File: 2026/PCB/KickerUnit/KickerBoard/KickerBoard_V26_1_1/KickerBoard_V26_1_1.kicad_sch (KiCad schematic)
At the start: 0 parts

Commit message: LT3751のシンボル作成
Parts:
- added U1: LT3751UFD, KickerUnit_LIB_SYM:QFN-20-1EP_LT3751UFD, symbol KickerUnit_LIB_SYM:LT3751UFD
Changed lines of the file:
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@@
 	(generator_version "9.0")
 	(paper "A4")
+	(symbol
+		(lib_id "KickerUnit_LIB_SYM:LT3751UFD")
+		(at 114.3 74.93 0)
+		(unit 1)
+		(exclude_from_sim no)
+		(in_bom yes)
+		(on_board yes)
+		(dnp no)
+		(property "Reference" "U1"
+			(at 96.774 99.568 0)
+			(effects
+				(font
+					(size 1.524 1.524)
+				)
+				(justify left)
+			)
+		)
+		(property "Value" "LT3751UFD"
+			(at 96.774 102.108 0)
+			(effects
+				(font
+					(size 1.524 1.524)
+				)
+				(justify left)
+			)
+		)
+		(property "Footprint" "KickerUnit_LIB_SYM:QFN-20-1EP_LT3751UFD"
+			(at 114.3 66.04 0)
+			(effects
+				(font
+					(size 1.27 1.27)
+					(italic yes)
+				)
+				(hide yes)
+			)
+		)
+		(property "Datasheet" "LT3751EUFD-PBF"
+			(at 115.824 68.326 0)
+			(effects
+				(font
+					(size 1.27 1.27)
+					(italic yes)
+				)
+				(hide yes)
+			)
+		)
+		(property "Description" ""
+			(at 114.3 74.93 0)
+			(effects
+				(font
+					(size 1.27 1.27)
+				)
+				(hide yes)
+			)
+		)
+		(pin "5"
+		)
+		(pin "6"
+		)
+		(pin "7"
+		)
+		(pin "11"
+		)
+		(pin "15"
+		)
+		(pin "12"
+		)
+		(pin "18"
+		)
+		(pin "19"
+		)
+		(pin "21"
+		)
+		(pin "17"
+		)
+		(pin "16"
+		)
+		(pin "13"
+		)
+		(pin "10"
+		)
+		(pin "9"
+		)
+		(pin "14"
+		)
+		(pin "8"
+		)
+		(pin "20"
+		)
+		(pin "1"
+		)
+		(pin "2"
+		)
+		(pin "3"
+		)
+		(pin "4"
+		)
+		(instances
+			(project ""
+				(path "/8c63cf69-5ffc-4db2-9a00-dda132db51ca"
+					(reference "U1")
+					(unit 1)
+				)
+			)
+		)
+	)
 	(sheet_instances
 		(path "/"

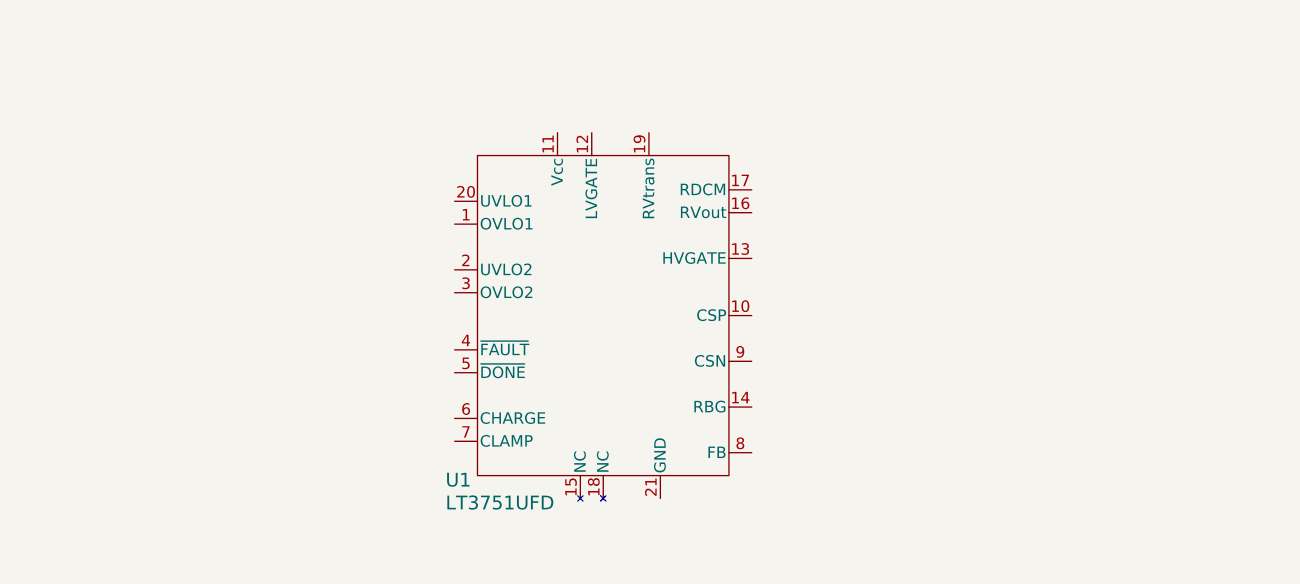
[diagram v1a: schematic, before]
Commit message: 昇圧素子の選定完了
ライブラリの追加
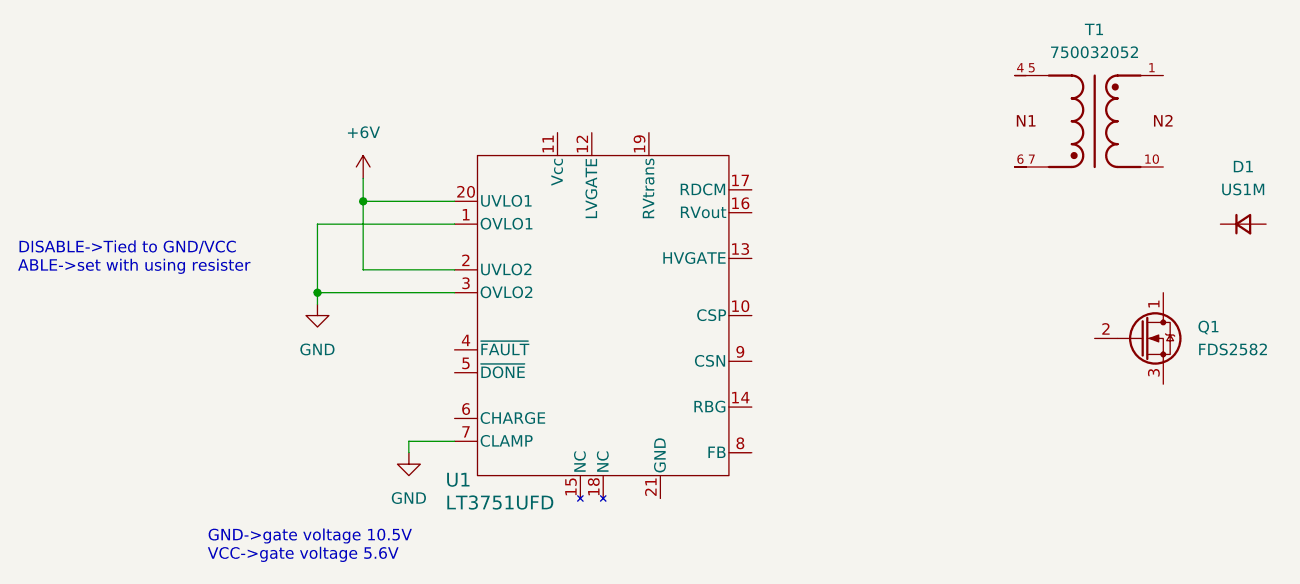
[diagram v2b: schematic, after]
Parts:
- added D1: US1M, Diode_SMD:D_SMA, symbol Device:D_Small
- added Q1: FDS2582, KickerUnit_LIB_SYM:FDS2582(SOIC8), symbol Transistor_FET_Other:Q_NMOS_Depletion_DGS
- added T1: 750032052, KickerUnit_LIB_SYM:WE-FB3751, symbol KickerUnit_LIB_SYM:750032052
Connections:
- net GND: now reaches U1.1 (OVLO1)
- net GND: now also U1.3 (OVLO2), U1.7 (CLAMP)
- net +6V: now reaches U1.2 (UVLO2)
- net +6V: now also U1.20 (UVLO1)
- new net: T1.4, T1.5
- new net: T1.6, T1.7
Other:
- note added: "DISABLE->Tied to GND/VCC ABLE->set with using resister"
- note added: "GND->gate voltage 10.5V VCC->gate voltage 5.6V"

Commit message: LT3751まわりの設計完了
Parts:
- added C1: 10nF/25V, symbol Device:C_Small
- added C10, C11, C3, C4: 10uF/50V, symbol Device:C_Small
- added C2: 10uF/25V, Resistor_SMD:R_0805_2012Metric_Pad1.20x1.40mm_HandSolder, symbol Device:C_Small
- added C5, C6: 1uF/50V, Resistor_SMD:R_0805_2012Metric_Pad1.20x1.40mm_HandSolder, symbol Device:C_Small
- added C8, C9: 100uF/50V, symbol Device:C_Polarized_Small
- added R1, R2: 100k, symbol Device:R_Small
- added R3: 1.3k, symbol Device:R_Small
- added R4: 18.2k, symbol Device:R_Small
- added R5, R6: 40.2k, symbol Device:R_Small
- added R7: 12m, Resistor_SMD:R_0805_2012Metric_Pad1.20x1.40mm_HandSolder, symbol Device:R_Small
- added R8: 274k, symbol Device:R_Small
- added R9: 1.13k, symbol Device:R_Small
- added TP1: Vds, symbol Connector:TestPoint
- added TP2: Vdd, symbol Connector:TestPoint
- added TP3: Vsec, symbol Connector:TestPoint
- added TP4: Vout, symbol Connector:TestPoint
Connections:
- net +6V: now also U1.11 (Vcc), C2.1, C5.1
- net GND: now also T1.10, U1.21 (GND), U1.9 (CSN), C1.2, C10.2, C11.2, C2.2, C3.2, C4.2, C5.2, C6.2, C8.2, C9.2, R3.2, R7.2, R9.2
- net at U1.10 (CSP): now also Q1.3 (S), R7.1
- net at U1.12 (LVGATE): now also Q1.2 (G), U1.13 (HVGATE)
- net at U1.14 (RBG): now also R3.1
- net at U1.16 (RVout): now also R5.2
- net at U1.17 (RDCM): now also R4.2
- net at U1.19 (RVtrans): now also R6.2
- net ~{nFault}: now reaches U1.4 (~{FAULT})
- net ~{nFault}: now also R1.1
- net ~{DONE}: now reaches U1.5 (~{DONE})
- net ~{DONE}: now also R2.1
- net CHARGE: now reaches U1.6 (CHARGE)
- net at U1.8 (FB): now also C1.1, R8.2, R9.1
- net at D1.1 (K): now also T1.1, TP3.1
- net Vout: now reaches D1.2 (A)
- net Vout: now also R8.1, TP4.1
- net at Q1.1 (D): now also T1.6, T1.7, R4.1, R5.1, TP1.1
- net VDD: now reaches T1.4, T1.5
- net VDD: now also C10.1, C11.1, C3.1, C4.1, C6.1, C8.1, C9.1, R6.1, TP2.1
- new net +3.3V: R1.2, R2.2
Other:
- note added: "302V"
- note added: "Ipk:9A(8.83A) Psense:0.19W"
- note added: "Vattely Voltage:24V (MAX 25V)"
- note added: "Vds:55.2V Iave:2.7A"
- note added: "Vrrm:552V Iave:0.5A"
- note removed: "GND->gate voltage 10.5V VCC->gate voltage 5.6V"
- moved on the sheet: D1, Q1, T1, U1

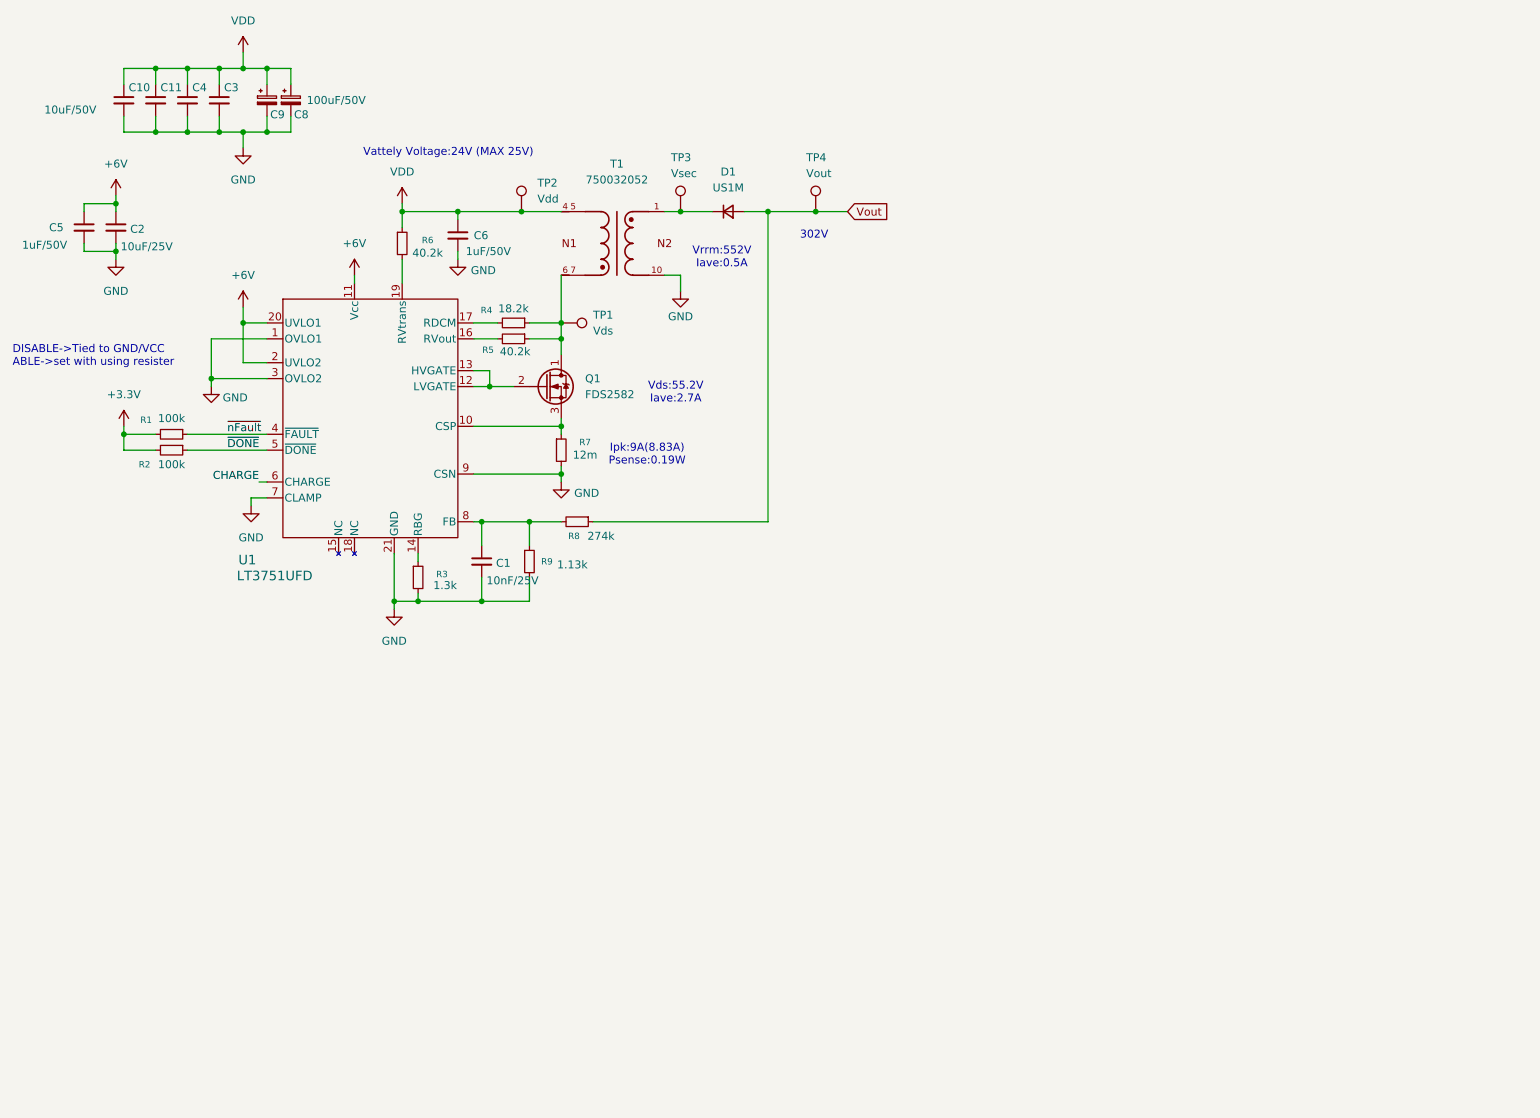
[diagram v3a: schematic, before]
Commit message: BoostCircuit.kicad_schの追加
階層シートに追加
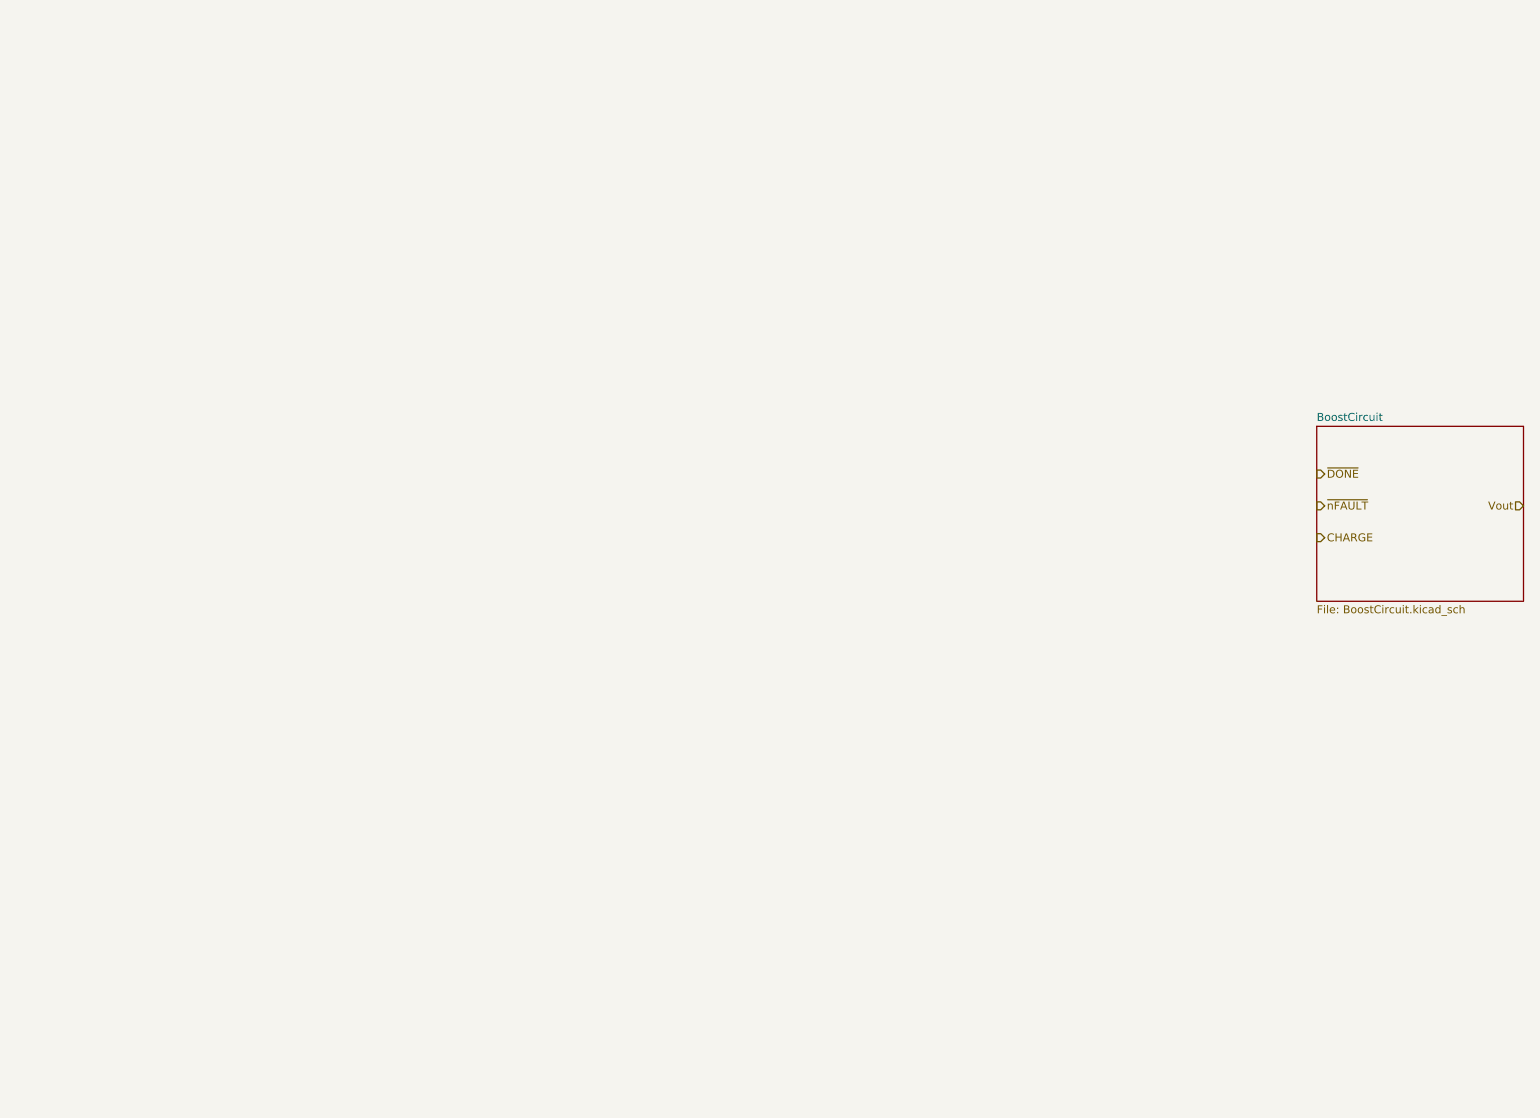
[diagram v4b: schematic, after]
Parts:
- removed C1: 10nF/25V, symbol Device:C_Small
- removed C10, C11, C3, C4: 10uF/50V, symbol Device:C_Small
- removed C2: 10uF/25V, Resistor_SMD:R_0805_2012Metric_Pad1.20x1.40mm_HandSolder, symbol Device:C_Small
- removed C5, C6: 1uF/50V, Resistor_SMD:R_0805_2012Metric_Pad1.20x1.40mm_HandSolder, symbol Device:C_Small
- removed C8, C9: 100uF/50V, symbol Device:C_Polarized_Small
- removed D1: US1M, Diode_SMD:D_SMA, symbol Device:D_Small
- removed Q1: FDS2582, KickerUnit_LIB_SYM:FDS2582(SOIC8), symbol Transistor_FET_Other:Q_NMOS_Depletion_DGS
- removed R1, R2: 100k, symbol Device:R_Small
- removed R3: 1.3k, symbol Device:R_Small
- removed R4: 18.2k, symbol Device:R_Small
- removed R5, R6: 40.2k, symbol Device:R_Small
- removed R7: 12m, Resistor_SMD:R_0805_2012Metric_Pad1.20x1.40mm_HandSolder, symbol Device:R_Small
- removed R8: 274k, symbol Device:R_Small
- removed R9: 1.13k, symbol Device:R_Small
- removed T1: 750032052, KickerUnit_LIB_SYM:WE-FB3751, symbol KickerUnit_LIB_SYM:750032052
- removed TP1: Vds, symbol Connector:TestPoint
- removed TP2: Vdd, symbol Connector:TestPoint
- removed TP3: Vsec, symbol Connector:TestPoint
- removed TP4: Vout, symbol Connector:TestPoint
- removed U1: LT3751UFD, KickerUnit_LIB_SYM:QFN-20-1EP_LT3751UFD, symbol KickerUnit_LIB_SYM:LT3751UFD
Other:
- added sheet BoostCircuit (BoostCircuit.kicad_sch)
- note removed: "302V"
- note removed: "DISABLE->Tied to GND/VCC ABLE->set with using resister"
- note removed: "Ipk:9A(8.83A) Psense:0.19W"
- note removed: "Vattely Voltage:24V (MAX 25V)"
- note removed: "Vds:55.2V Iave:2.7A"
- note removed: "Vrrm:552V Iave:0.5A"

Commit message: 6.5V降圧DCDCの追加
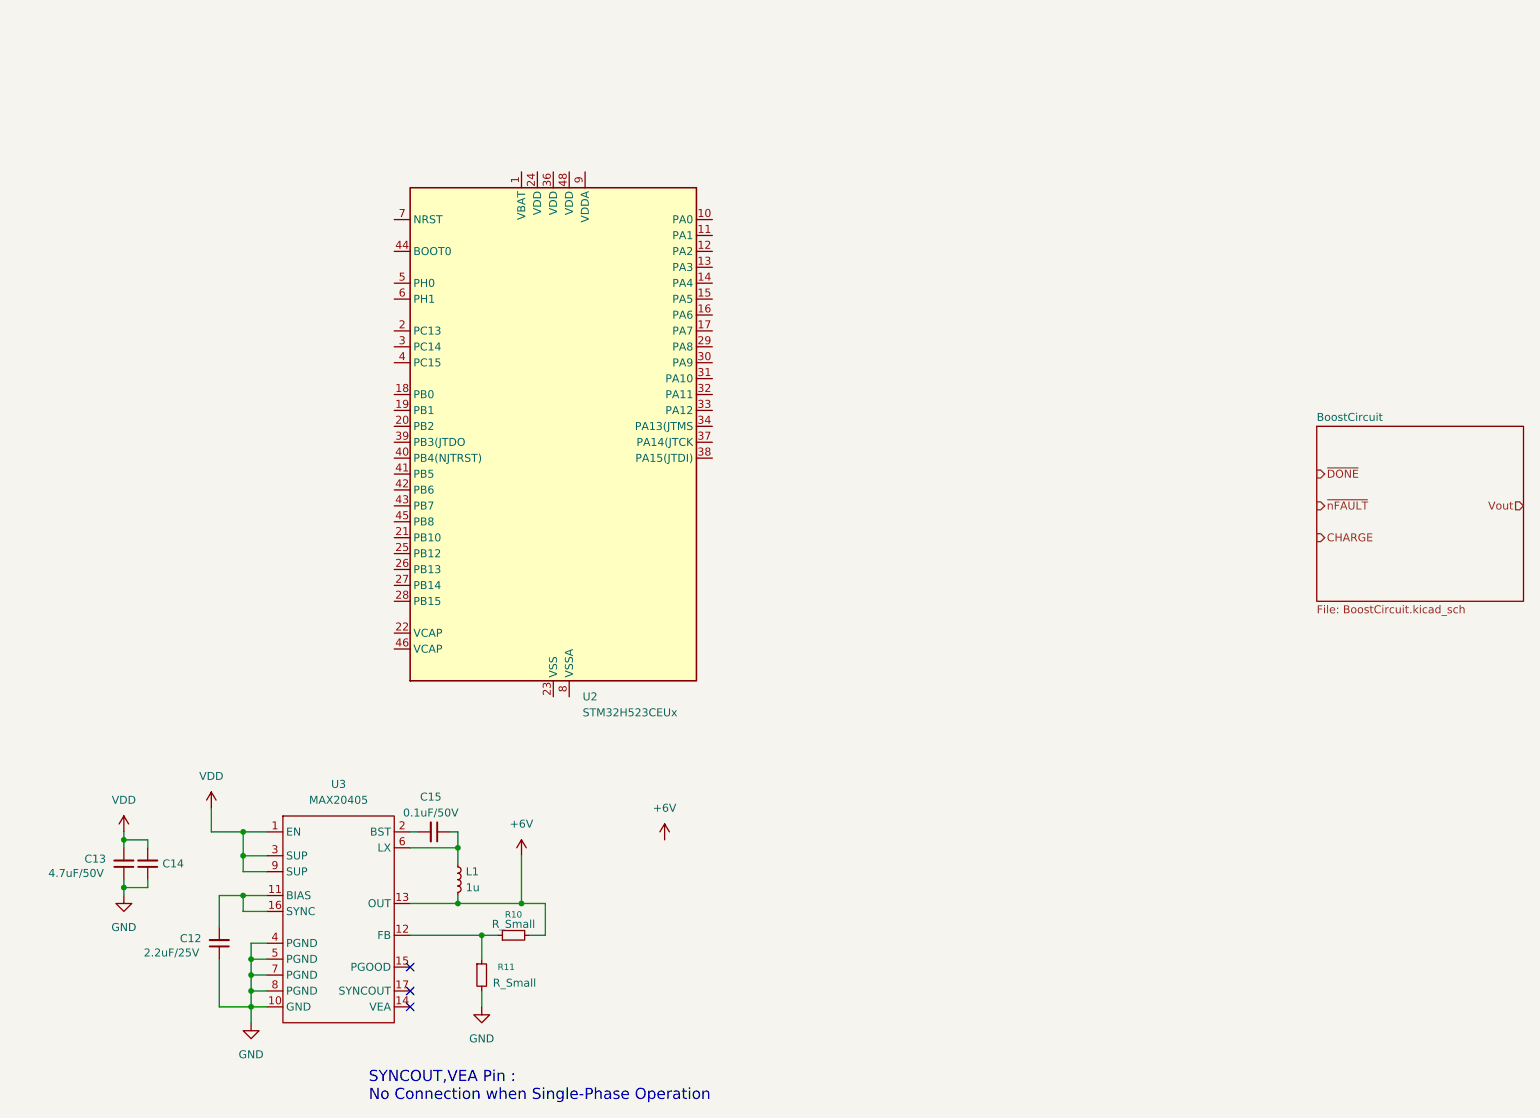
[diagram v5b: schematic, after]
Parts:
- added C12, C14: 2.2uF/25V, symbol Device:C_Small
- added C13: 4.7uF/50V, symbol Device:C_Small
- added C15: 0.1uF/50V, symbol Device:C_Small
- added L1: 1u, symbol Device:L_Small
- added R10, R11: R_Small, symbol Device:R_Small
- added U2: STM32H523CEUx, Package_DFN_QFN:QFN-48-1EP_7x7mm_P0.5mm_EP5.6x5.6mm, symbol MCU_ST_STM32H5:STM32H523CEUx
- added U3: MAX20405, symbol KickerUnit_LIB_SYM:MAX20405
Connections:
- new net: R10.1, R11.1, U3.12 (FB)
- new net: C15.1, L1.1, U3.6 (LX)
- new net: C15.2, U3.2 (BST)
- new net: C12.2, U3.11 (BIAS), U3.16 (SYNC)
- new net: U2.23 (VSS), U2.35 (VSS), U2.47 (VSS), U2.49 (VSS)
- new net +6V: L1.2, R10.2, U3.13 (OUT)
- new net GND: C12.1, C13.1, C14.1, R11.2, U3.10 (GND), U3.4 (PGND), U3.5 (PGND), U3.7 (PGND), U3.8 (PGND)
- new net VDD: C13.2, C14.2, U3.1 (EN), U3.3 (SUP), U3.9 (SUP)
- no-connect marks 0 -> 3
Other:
- note added: "SYNCOUT,VEA Pin : No Connection when Single-Phase Operation"
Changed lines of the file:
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@@
 	(generator_version "9.0")
 	(paper "A4")
-	(hierarchical_label "~{nFAULT}"
-		(shape output)
-		(at 223.52 93.98 0)
-		(effects
-			(font
-				(size 1.27 1.27)
-			)
-			(justify left)
-		)
-	)
-	(hierarchical_label "~{DONE}"
-		(shape output)
-		(at 223.52 88.9 0)
-		(effects
-			(font
-				(size 1.27 1.27)
-			)
-			(justify left)
-		)
-	)
-	(hierarchical_label "CHARGE"
-		(shape output)
-		(at 223.52 99.06 0)
-		(effects
-			(font
-				(size 1.27 1.27)
-			)
-			(justify left)
-		)
-	)
-	(hierarchical_label "Vout"
-		(shape input)
-		(at 256.54 93.98 180)
-		(effects
-			(font
-				(size 1.27 1.27)
-			)
-			(justify right)
-		)
-	)
-	(sheet
-		(at 223.52 81.28)
-		(size 33.02 27.94)
-		(exclude_from_sim no)
-		(in_bom yes)
-		(on_board yes)
-		(dnp no)
-		(fields_autoplaced yes)
-		(stroke
-			(width 0.1524)
-			(type solid)
-		)
-		(fill
-			(color 0 0 0 0.0000)
-		)
-		(property "Sheetname" "BoostCircuit"
-			(at 223.52 80.5684 0)
-			(effects
-				(font
-					(size 1.27 1.27)
-				)
-				(justify left bottom)
-			)
-		)
-		(property "Sheetfile" "BoostCircuit.kicad_sch"
-			(at 223.52 109.8046 0)
-			(effects
-				(font
-					(size 1.27 1.27)
-				)
-				(justify left top)
-			)
-		)
-		(instances
-			(project "KickerBoard_V26_1_1"
-				(path "/8c63cf69-5ffc-4db2-9a00-dda132db51ca"
-					(page "2")
-				)
-			)
-		)
-	)
-	(sheet_instances
-		(path "/"
-			(page "1")
-		)
-	)
-	(embedded_fonts no)
-)
